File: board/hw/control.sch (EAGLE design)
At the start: 35 parts, among them T1 pn2222a, T2 pn2222a, T3 pn2222a, T4 pn2222a, T5 pn2222a, T6 pn2222a, T7 pn2222a, T8 pn2222a

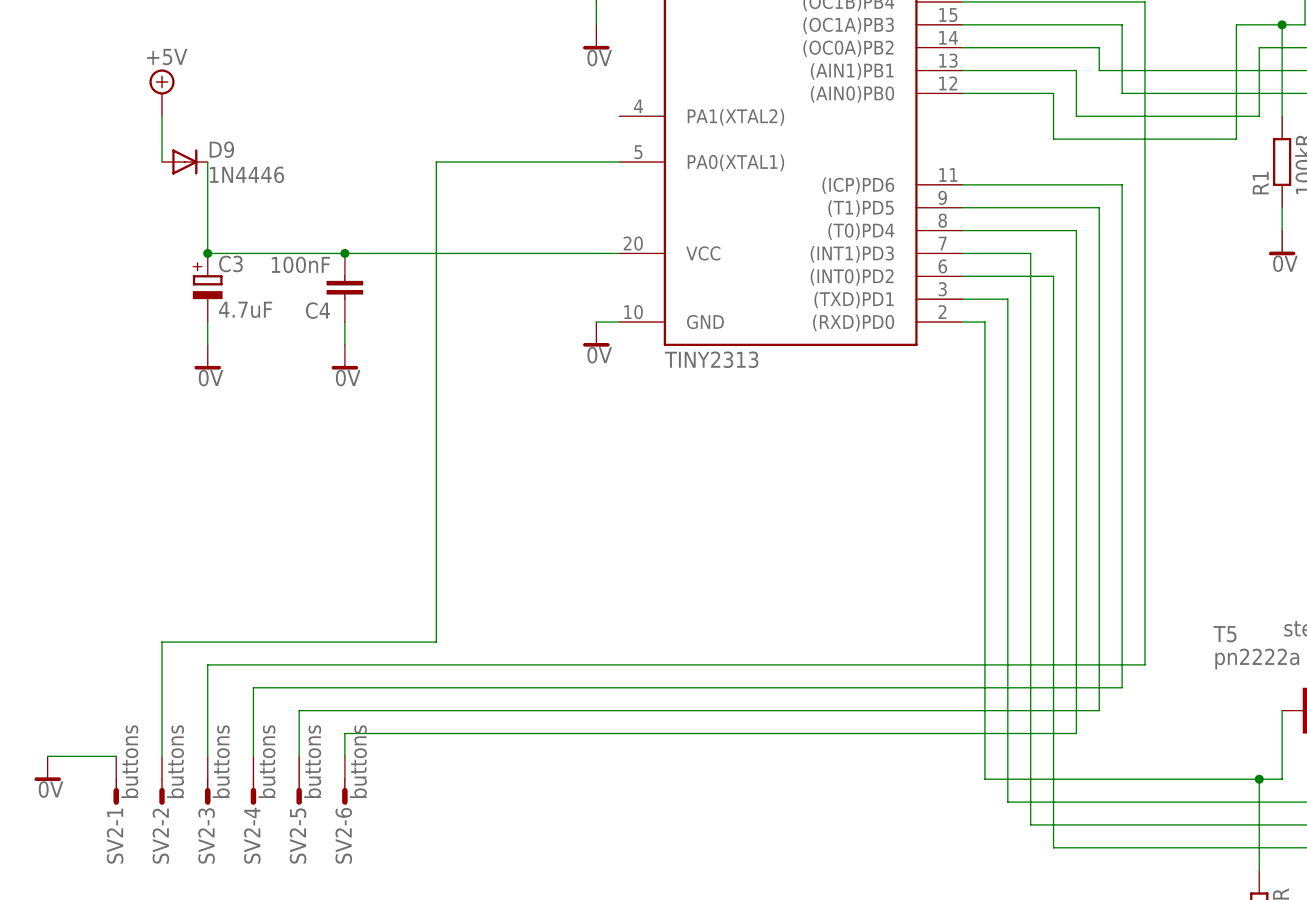
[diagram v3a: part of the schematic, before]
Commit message: added missing pull-up 100k Rs for all buttons
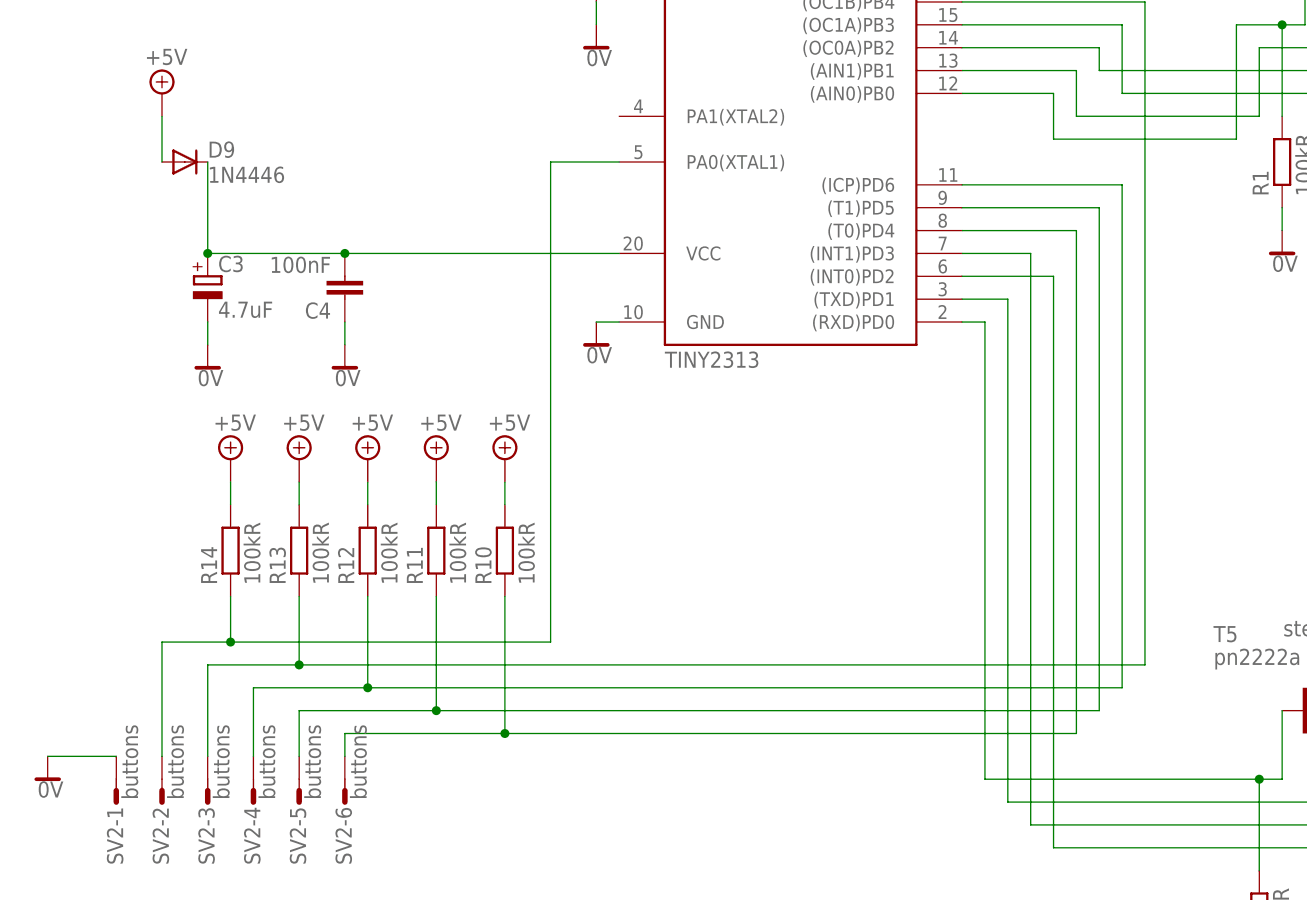
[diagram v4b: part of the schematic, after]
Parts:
- added R10, R11, R12, R13, R14: 100kR, rcl:R-EU_MELF0204W
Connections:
- net +5V: now also R10.2, R11.2, R12.2, R13.2, R14.2
- net N$22: now also R11.1
- net N$23: now also R12.1
- net N$24: now also R13.1
- net N$25: now also R14.1
- net N$3: now also R10.1
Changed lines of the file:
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@@
 <part name="SUPPLY2" library="supply2" deviceset="+5V" device=""/>
 <part name="SUPPLY41" library="supply2" deviceset="0V" device=""/>
+<part name="R10" library="rcl" deviceset="R-EU_" device="MELF0204W" value="100kR"/>
+<part name="R11" library="rcl" deviceset="R-EU_" device="MELF0204W" value="100kR"/>
+<part name="R12" library="rcl" deviceset="R-EU_" device="MELF0204W" value="100kR"/>
+<part name="R13" library="rcl" deviceset="R-EU_" device="MELF0204W" value="100kR"/>
+<part name="R14" library="rcl" deviceset="R-EU_" device="MELF0204W" value="100kR"/>
+<part name="SUPPLY42" library="supply2" deviceset="+5V" device=""/>
+<part name="SUPPLY43" library="supply2" deviceset="+5V" device=""/>
+<part name="SUPPLY44" library="supply2" deviceset="+5V" device=""/>
+<part name="SUPPLY45" library="supply2" deviceset="+5V" device=""/>
+<part name="SUPPLY46" library="supply2" deviceset="+5V" device=""/>
 </parts>
 <sheets>
@@
 <instance part="SUPPLY2" gate="+5V" x="-12.7" y="93.98"/>
 <instance part="SUPPLY41" gate="0V" x="-12.7" y="83.82"/>
+<instance part="R10" gate="G$1" x="30.48" y="5.08" rot="R90"/>
+<instance part="R11" gate="G$1" x="22.86" y="5.08" rot="R90"/>
+<instance part="R12" gate="G$1" x="15.24" y="5.08" rot="R90"/>
+<instance part="R13" gate="G$1" x="7.62" y="5.08" rot="R90"/>
+<instance part="R14" gate="G$1" x="0" y="5.08" rot="R90"/>
+<instance part="SUPPLY42" gate="+5V" x="30.48" y="15.24"/>
+<instance part="SUPPLY43" gate="+5V" x="22.86" y="15.24"/>
+<instance part="SUPPLY44" gate="+5V" x="15.24" y="15.24"/>
+<instance part="SUPPLY45" gate="+5V" x="7.62" y="15.24"/>
+<instance part="SUPPLY46" gate="+5V" x="0" y="15.24"/>
 </instances>
 <busses>
@@
 <pinref part="SUPPLY2" gate="+5V" pin="+5V"/>
 <wire x1="-12.7" y1="91.44" x2="-15.24" y2="91.44" width="0.1524" layer="91"/>
+</segment>
+<segment>
+<pinref part="R10" gate="G$1" pin="2"/>
+<pinref part="SUPPLY42" gate="+5V" pin="+5V"/>
+<wire x1="30.48" y1="12.7" x2="30.48" y2="10.16" width="0.1524" layer="91"/>
+</segment>
+<segment>
+<pinref part="R11" gate="G$1" pin="2"/>
+<pinref part="SUPPLY43" gate="+5V" pin="+5V"/>
+<wire x1="22.86" y1="12.7" x2="22.86" y2="10.16" width="0.1524" layer="91"/>
+</segment>
+<segment>
+<pinref part="R12" gate="G$1" pin="2"/>
+<pinref part="SUPPLY44" gate="+5V" pin="+5V"/>
+<wire x1="15.24" y1="12.7" x2="15.24" y2="10.16" width="0.1524" layer="91"/>
+</segment>
+<segment>
+<pinref part="R13" gate="G$1" pin="2"/>
+<pinref part="SUPPLY45" gate="+5V" pin="+5V"/>
+<wire x1="7.62" y1="12.7" x2="7.62" y2="10.16" width="0.1524" layer="91"/>
+</segment>
+<segment>
+<pinref part="R14" gate="G$1" pin="2"/>
+<pinref part="SUPPLY46" gate="+5V" pin="+5V"/>
+<wire x1="0" y1="12.7" x2="0" y2="10.16" width="0.1524" layer="91"/>
 </segment>
 </net>
@@
 <wire x1="93.98" y1="40.64" x2="93.98" y2="-15.24" width="0.1524" layer="91"/>
 <pinref part="SV2" gate="-6" pin="S"/>
-<wire x1="93.98" y1="-15.24" x2="12.7" y2="-15.24" width="0.1524" layer="91"/>
+<wire x1="93.98" y1="-15.24" x2="30.48" y2="-15.24" width="0.1524" layer="91"/>
+<wire x1="30.48" y1="-15.24" x2="12.7" y2="-15.24" width="0.1524" layer="91"/>
 <wire x1="12.7" y1="-15.24" x2="12.7" y2="-17.78" width="0.1524" layer="91"/>
+<pinref part="R10" gate="G$1" pin="1"/>
+<wire x1="30.48" y1="0" x2="30.48" y2="-15.24" width="0.1524" layer="91"/>
+<junction x="30.48" y="-15.24"/>
 </segment>
 </net>
@@
 <pinref part="SV2" gate="-5" pin="S"/>
 <wire x1="7.62" y1="-17.78" x2="7.62" y2="-12.7" width="0.1524" layer="91"/>
-<wire x1="7.62" y1="-12.7" x2="96.52" y2="-12.7" width="0.1524" layer="91"/>
+<wire x1="7.62" y1="-12.7" x2="22.86" y2="-12.7" width="0.1524" layer="91"/>
+<wire x1="22.86" y1="-12.7" x2="96.52" y2="-12.7" width="0.1524" layer="91"/>
 <wire x1="96.52" y1="-12.7" x2="96.52" y2="43.18" width="0.1524" layer="91"/>
 <pinref part="U$1" gate="G$1" pin="(T1)PD5"/>
 <wire x1="96.52" y1="43.18" x2="81.28" y2="43.18" width="0.1524" layer="91"/>
+<pinref part="R11" gate="G$1" pin="1"/>
+<wire x1="22.86" y1="0" x2="22.86" y2="-12.7" width="0.1524" layer="91"/>
+<junction x="22.86" y="-12.7"/>
 </segment>
 </net>
@@
 <wire x1="81.28" y1="45.72" x2="99.06" y2="45.72" width="0.1524" layer="91"/>
 <wire x1="99.06" y1="45.72" x2="99.06" y2="-10.16" width="0.1524" layer="91"/>
-<wire x1="99.06" y1="-10.16" x2="2.54" y2="-10.16" width="0.1524" layer="91"/>
+<wire x1="99.06" y1="-10.16" x2="15.24" y2="-10.16" width="0.1524" layer="91"/>
+<wire x1="15.24" y1="-10.16" x2="2.54" y2="-10.16" width="0.1524" layer="91"/>
 <wire x1="2.54" y1="-10.16" x2="2.54" y2="-17.78" width="0.1524" layer="91"/>
 <pinref part="SV2" gate="-4" pin="S"/>
+<pinref part="R12" gate="G$1" pin="1"/>
+<wire x1="15.24" y1="0" x2="15.24" y2="-10.16" width="0.1524" layer="91"/>
+<junction x="15.24" y="-10.16"/>
 </segment>
 </net>
@@
 <wire x1="101.6" y1="66.04" x2="101.6" y2="-7.62" width="0.1524" layer="91"/>
 <pinref part="SV2" gate="-3" pin="S"/>
-<wire x1="101.6" y1="-7.62" x2="-2.54" y2="-7.62" width="0.1524" layer="91"/>
+<wire x1="101.6" y1="-7.62" x2="7.62" y2="-7.62" width="0.1524" layer="91"/>
+<wire x1="7.62" y1="-7.62" x2="-2.54" y2="-7.62" width="0.1524" layer="91"/>
 <wire x1="-2.54" y1="-7.62" x2="-2.54" y2="-17.78" width="0.1524" layer="91"/>
+<pinref part="R13" gate="G$1" pin="1"/>
+<wire x1="7.62" y1="0" x2="7.62" y2="-7.62" width="0.1524" layer="91"/>
+<junction x="7.62" y="-7.62"/>
 </segment>
 </net>
@@
 <segment>
 <pinref part="U$1" gate="G$1" pin="PA0(XTAL1)"/>
-<wire x1="43.18" y1="48.26" x2="22.86" y2="48.26" width="0.1524" layer="91"/>
-<wire x1="22.86" y1="48.26" x2="22.86" y2="-5.08" width="0.1524" layer="91"/>
+<wire x1="43.18" y1="48.26" x2="35.56" y2="48.26" width="0.1524" layer="91"/>
+<wire x1="35.56" y1="48.26" x2="35.56" y2="-5.08" width="0.1524" layer="91"/>
 <pinref part="SV2" gate="-2" pin="S"/>
-<wire x1="22.86" y1="-5.08" x2="-7.62" y2="-5.08" width="0.1524" layer="91"/>
+<wire x1="35.56" y1="-5.08" x2="0" y2="-5.08" width="0.1524" layer="91"/>
+<wire x1="0" y1="-5.08" x2="-7.62" y2="-5.08" width="0.1524" layer="91"/>
 <wire x1="-7.62" y1="-5.08" x2="-7.62" y2="-17.78" width="0.1524" layer="91"/>
-</segment>
-</net>
+<pinref part="R14" gate="G$1" pin="1"/>
+<wire x1="0" y1="0" x2="0" y2="-5.08" width="0.1524" layer="91"/>
+<junction x="0" y="-5.08"/>
+</segment>
+</net>
